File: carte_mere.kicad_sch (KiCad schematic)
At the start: 22 parts, among them J10 Conn_01x02_Pin, J11 Conn_01x02_Pin, J12 Conn_01x02_Pin, J13 Conn_01x02_Pin, J14 Conn_01x02, J20 Conn_01x04, J23 Conn_01x02

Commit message: clean
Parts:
- added J24: Conn_01x02, Connector_Molex:Molex_KK-254_AE-6410-02A_1x02_P2.54mm_Vertical, symbol Connector_Generic:Conn_01x02
- added R126, R127, R128, R129, R130, R131, R132, R133, R134, R135, R136, R137, R138, R139, R140, R141, R142, R143, R144, R145, R146, R147, R148, R149, R150: 100R, Capacitor_SMD:C_0402_1005Metric, symbol Device:R
- added R151: 1k, Capacitor_SMD:C_0402_1005Metric, symbol Device:R
- added R152: 2k, Capacitor_SMD:C_0402_1005Metric, symbol Device:R
- added SPARE_1, SPARE_2, SPARE_3: Conn_02x05_Odd_Even, Connector_PinSocket_2.54mm:PinSocket_2x05_P2.54mm_Vertical, symbol Connector_Generic:Conn_02x05_Odd_Even
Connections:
- net 3.3V: now also SPARE_1.5 (Pin_5), SPARE_2.5 (Pin_5)
- net 5V: now also R151.1, SPARE_3.5 (Pin_5)
- net AU: now also JP1.JP2_36 (M20); no longer JP1.JP2_34 (F20)
- net GND: now also J24.2 (Pin_2), R152.2, SPARE_1.6 (Pin_6), SPARE_2.6 (Pin_6), SPARE_3.6 (Pin_6)
- net QEI_1_A: now also JP1.JP2_33 (F19); no longer JP1.JP2_23 (K16)
- net QEI_1_B: now also JP1.JP2_34 (F20); no longer JP1.JP2_25 (C20)
- net QEI_1_X: now also JP1.JP2_35 (M19); no longer JP1.JP2_27 (G17)
- net QEI_2_A: now also JP1.JP2_28 (G18); no longer JP1.JP2_31 (L19)
- net QEI_2_B: now also JP1.JP2_27 (G17); no longer JP1.JP2_33 (F19)
- net QEI_2_X: now also JP1.JP2_32 (L20); no longer JP1.JP2_35 (M19)
- net QEI_3_A: now also JP1.JP2_25 (C20); no longer JP1.JP2_28 (G18)
- net QEI_3_B: now also JP1.JP2_26 (B20); no longer JP1.JP2_32 (L20)
- net QEI_3_X: now also JP1.JP2_23 (K16); no longer JP1.JP2_26 (B20)
- net Tirette: now also JP1.JP2_31 (L19); no longer JP1.JP2_36 (M20)
- net spare3_5: now reaches JP1.JP1_10 (Y19)
- net spare3_5: now also R144.1
- net spare3_2: now reaches JP1.JP1_13 (Y16)
- net spare3_2: now also R146.2
- net spare3_1: now reaches JP1.JP1_14 (Y17)
- net spare3_1: now also R142.1
- net spare3_6: now reaches JP1.JP1_15 (V17)
- net spare3_6: now also R148.2
- net spare3_4: now reaches JP1.JP1_16 (V18)
- net spare3_4: now also R147.2
- net spare2_6: now reaches JP1.JP1_17 (W14)
- net spare2_6: now also R140.2
- net spare2_4: now reaches JP1.JP1_18 (Y14)
- net spare2_4: now also R139.2
- net spare2_7: now reaches JP1.JP1_19 (V16)
- net spare2_7: now also R137.1
- net spare2_8: now reaches JP1.JP1_20 (W16)
- net spare2_8: now also R141.2
- net spare2_3: now reaches JP1.JP1_21 (T17)
- net spare2_3: now also R135.1
- net spare2_5: now reaches JP1.JP1_22 (R18)
- net spare2_5: now also R136.1
- net spare2_2: now reaches JP1.JP1_23 (V12)
- net spare2_2: now also R138.2
- net spare2_1: now reaches JP1.JP1_24 (W13)
- net spare2_1: now also R134.1
- net spare1_6: now reaches JP1.JP1_25 (T14)
- net spare1_6: now also R132.2
- net spare1_4: now reaches JP1.JP1_26 (T15)
- net spare1_4: now also R131.2
- net spare1_7: now reaches JP1.JP1_27 (T11)
- net spare1_7: now also R129.1
- net spare1_8: now reaches JP1.JP1_28 (T10)
- net spare1_8: now also R130.2
- net spare1_3: now reaches JP1.JP1_31 (V15)
- net spare1_3: now also R127.1
- net spare1_5: now reaches JP1.JP1_32 (W15)
- net spare1_5: now also R128.1
- net spare1_1: now reaches JP1.JP1_33 (P14)
- net spare1_1: now also R126.1
- net spare1_2: now reaches JP1.JP1_34 (R14)
- net spare1_2: now also R133.2
- net spare3_8: now reaches JP1.JP1_6 (U17)
- net spare3_8: now also R149.2
- net spare3_7: now reaches JP1.JP1_8 (W19)
- net spare3_7: now also R145.1
- net spare3_3: now reaches JP1.JP1_9 (Y18)
- net spare3_3: now also R143.1
- net TEAM: now reaches JP1.JP2_38 (J19)
- net TEAM: now also R150.1
- new net: R140.1, SPARE_2.8 (Pin_8)
- new net: R149.1, SPARE_3.10 (Pin_10)
- new net: R127.2, SPARE_1.3 (Pin_3)
- new net: R129.2, SPARE_1.9 (Pin_9)
- new net: R141.1, SPARE_2.10 (Pin_10)
- new net: J24.1 (Pin_1), R150.2, R151.2, R152.1
- new net: R131.1, SPARE_1.4 (Pin_4)
- new net: R139.1, SPARE_2.4 (Pin_4)
- new net: R135.2, SPARE_2.3 (Pin_3)
- new net: R133.1, SPARE_1.2 (Pin_2)
- new net: R130.1, SPARE_1.10 (Pin_10)
- new net: R126.2, SPARE_1.1 (Pin_1)
- new net: R128.2, SPARE_1.7 (Pin_7)
- new net: R132.1, SPARE_1.8 (Pin_8)
- new net: R134.2, SPARE_2.1 (Pin_1)
- new net: R138.1, SPARE_2.2 (Pin_2)
- new net: R136.2, SPARE_2.7 (Pin_7)
- new net: R137.2, SPARE_2.9 (Pin_9)
- new net: R142.2, SPARE_3.1 (Pin_1)
- new net: R146.1, SPARE_3.2 (Pin_2)
- new net: R143.2, SPARE_3.3 (Pin_3)
- new net: R147.1, SPARE_3.4 (Pin_4)
- new net: R144.2, SPARE_3.7 (Pin_7)
- new net: R148.1, SPARE_3.8 (Pin_8)
- new net: R145.2, SPARE_3.9 (Pin_9)
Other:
- note added: "Nappe spare"
- note added: "TEAM"
- moved on the sheet: J13, R118, R119, R121, R122

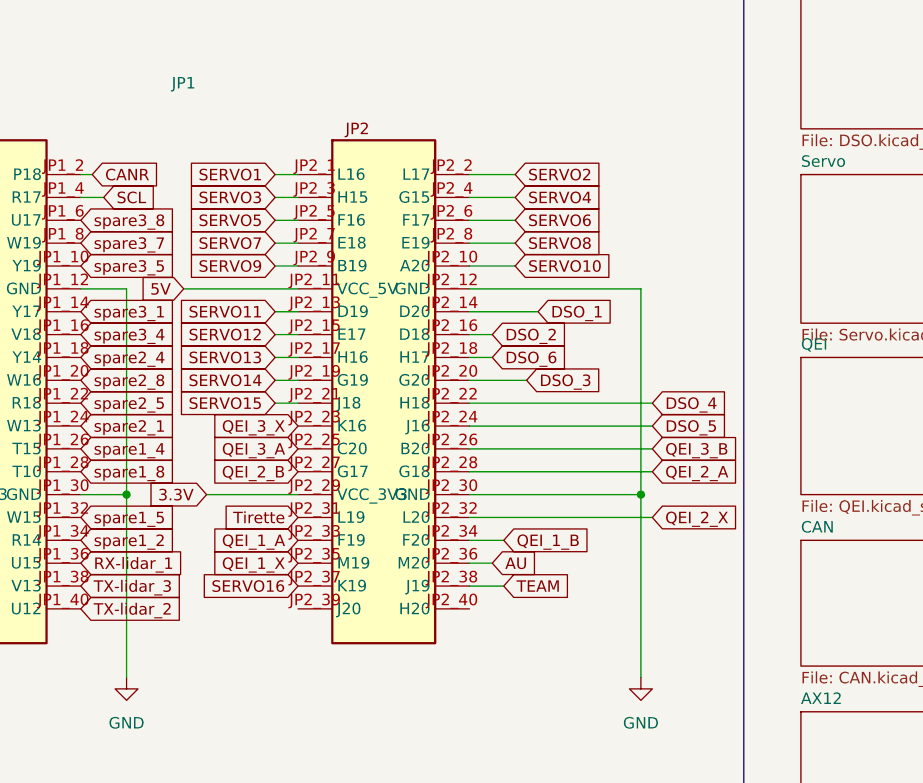
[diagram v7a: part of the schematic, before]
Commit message: fix issue on zynq footprint
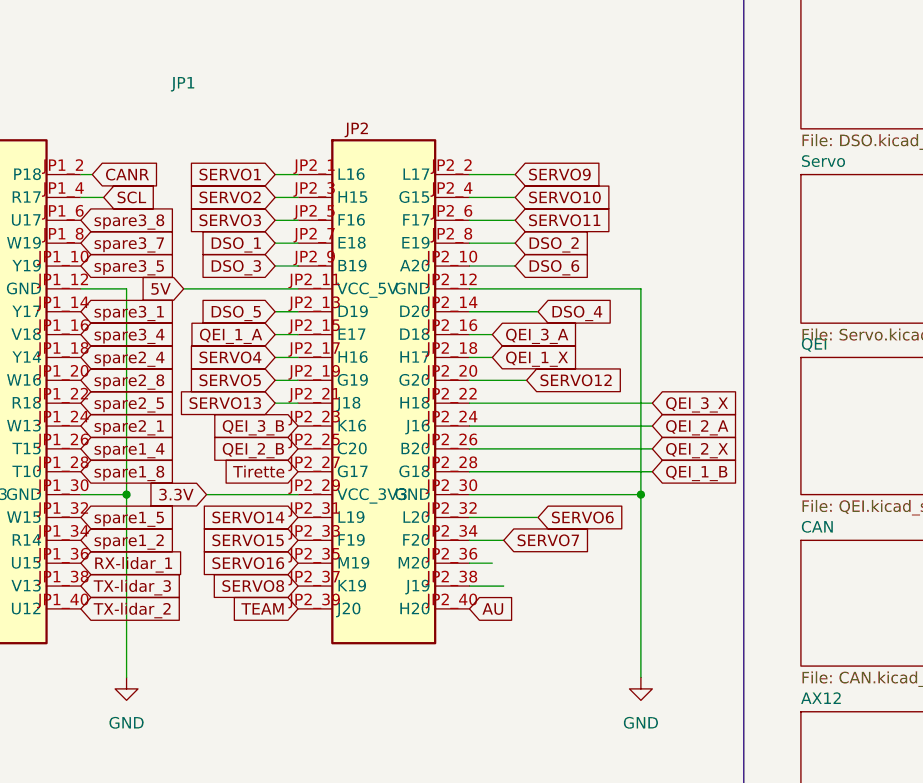
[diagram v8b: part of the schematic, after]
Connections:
- net AU: now also JP1.JP2_40 (H20); no longer JP1.JP2_36 (M20)
- net DSO_1: now also JP1.JP2_7 (E18); no longer JP1.JP2_14 (D20)
- net DSO_2: now also JP1.JP2_8 (E19); no longer JP1.JP2_16 (D18)
- net DSO_3: now also JP1.JP2_9 (B19); no longer JP1.JP2_20 (G20)
- net DSO_4: now also JP1.JP2_14 (D20); no longer JP1.JP2_22 (H18)
- net DSO_5: now also JP1.JP2_13 (D19); no longer JP1.JP2_24 (J16)
- net DSO_6: now also JP1.JP2_10 (A20); no longer JP1.JP2_18 (H17)
- net QEI_1_A: now also JP1.JP2_15 (E17); no longer JP1.JP2_33 (F19)
- net QEI_1_B: now also JP1.JP2_28 (G18); no longer JP1.JP2_34 (F20)
- net QEI_1_X: now also JP1.JP2_18 (H17); no longer JP1.JP2_35 (M19)
- net QEI_2_A: now also JP1.JP2_24 (J16); no longer JP1.JP2_28 (G18)
- net QEI_2_B: now also JP1.JP2_25 (C20); no longer JP1.JP2_27 (G17)
- net QEI_2_X: now also JP1.JP2_26 (B20); no longer JP1.JP2_32 (L20)
- net QEI_3_A: now also JP1.JP2_16 (D18); no longer JP1.JP2_25 (C20)
- net QEI_3_B: now also JP1.JP2_23 (K16); no longer JP1.JP2_26 (B20)
- net QEI_3_X: now also JP1.JP2_22 (H18); no longer JP1.JP2_23 (K16)
- net SERVO10: now also JP1.JP2_4 (G15); no longer JP1.JP2_10 (A20)
- net SERVO11: now also JP1.JP2_6 (F17); no longer JP1.JP2_13 (D19)
- net SERVO12: now also JP1.JP2_20 (G20); no longer JP1.JP2_15 (E17)
- net SERVO13: now also JP1.JP2_21 (J18); no longer JP1.JP2_17 (H16)
- net SERVO14: now also JP1.JP2_31 (L19); no longer JP1.JP2_19 (G19)
- net SERVO15: now also JP1.JP2_33 (F19); no longer JP1.JP2_21 (J18)
- net SERVO16: now also JP1.JP2_35 (M19); no longer JP1.JP2_37 (K19)
- net SERVO2: now also JP1.JP2_3 (H15); no longer JP1.JP2_2 (L17)
- net SERVO3: now also JP1.JP2_5 (F16); no longer JP1.JP2_3 (H15)
- net SERVO4: now also JP1.JP2_17 (H16); no longer JP1.JP2_4 (G15)
- net SERVO5: now also JP1.JP2_19 (G19); no longer JP1.JP2_5 (F16)
- net SERVO6: now also JP1.JP2_32 (L20); no longer JP1.JP2_6 (F17)
- net SERVO7: now also JP1.JP2_34 (F20); no longer JP1.JP2_7 (E18)
- net SERVO8: now also JP1.JP2_37 (K19); no longer JP1.JP2_8 (E19)
- net SERVO9: now also JP1.JP2_2 (L17); no longer JP1.JP2_9 (B19)
- net TEAM: now also JP1.JP2_39 (J20); no longer JP1.JP2_38 (J19)
- net Tirette: now also JP1.JP2_27 (G17); no longer JP1.JP2_31 (L19)
